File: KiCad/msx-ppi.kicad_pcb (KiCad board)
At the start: 2 copper layers, 85.1 x 63.9 mm, 17 parts, among them J1 Conn_02x13_Odd_Even, P1 CONN_02X25, Q1 BC547, SW1 DIPx8, U1 74HCT138, U2 74HCT32, U3 82C55A

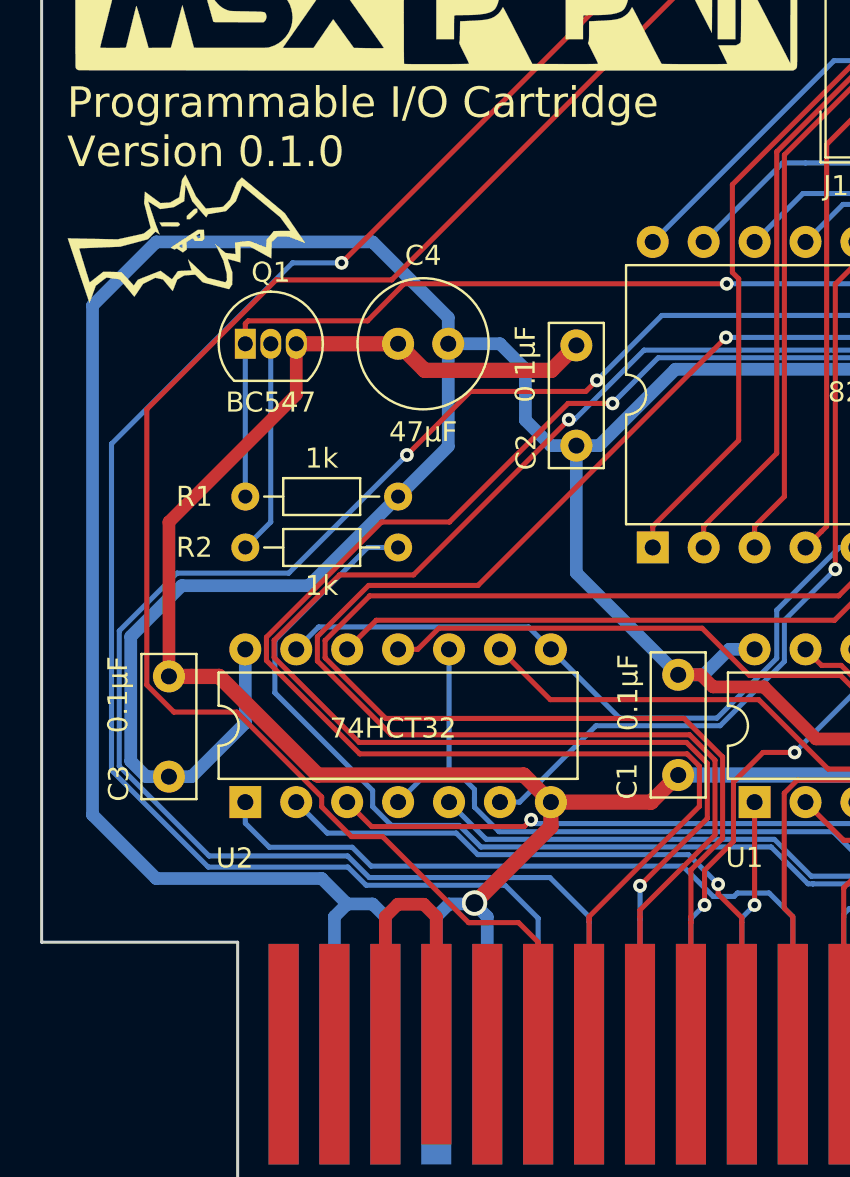
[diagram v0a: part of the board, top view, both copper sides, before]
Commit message: Changed Q1 footprint
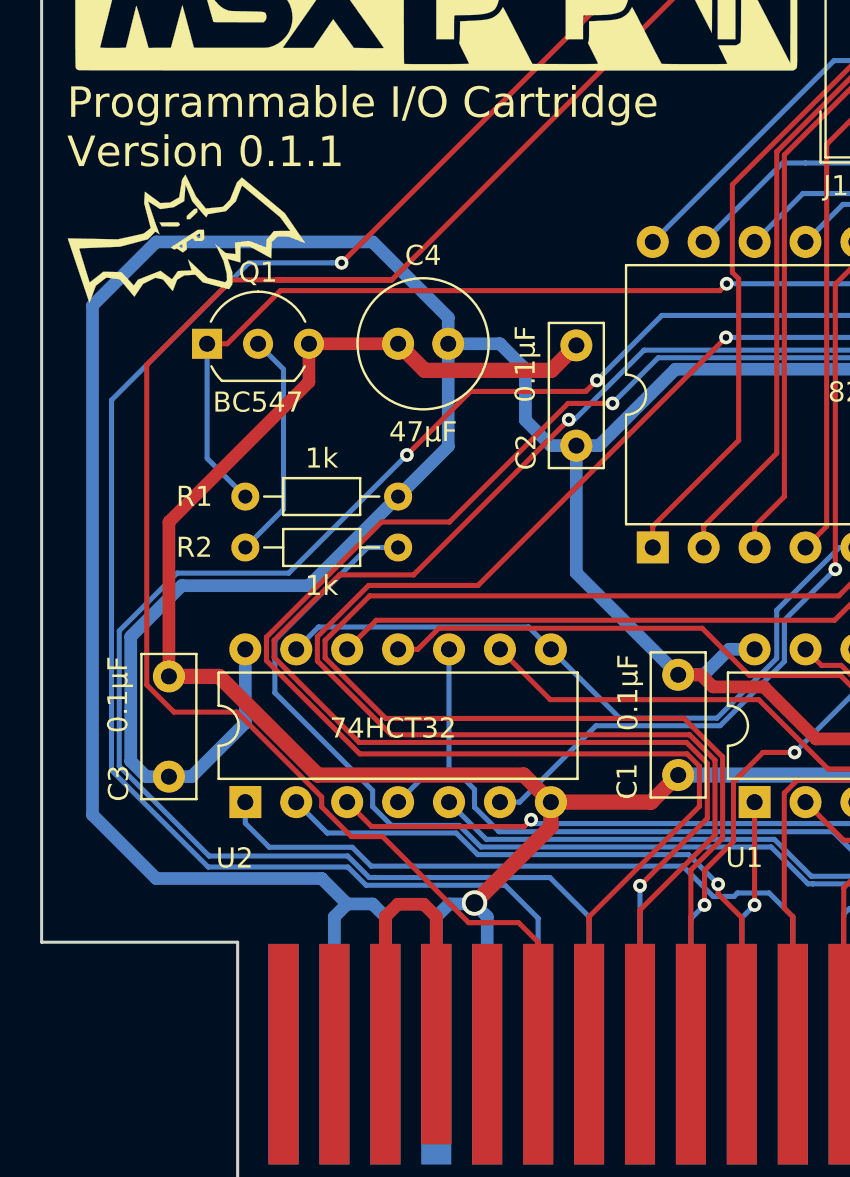
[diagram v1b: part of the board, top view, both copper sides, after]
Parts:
- Q1: footprint Package_TO_SOT_THT:TO-92_Inline -> Package_TO_SOT_THT:TO-92_Inline_Wide
- moved Q1 1.91 mm to (116.2, 87.0)
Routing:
- net D6: track 117.1 -> 124.2 mm
- net Net-(Q1-Pad1): track 43.3 -> 45.4 mm
- net D7: track 125.6 -> 126.9 mm
- net Net-(Q1-Pad2): track 10.7 -> 11.5 mm
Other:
- board text added: "Programmable I/O Cartridge Version 0.1.1"
- board text removed: "Programmable I/O Cartridge Version 0.1.0"

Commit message: Changed R2 value to 10k (was 1k)
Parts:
- R1: value 1k -> 10k
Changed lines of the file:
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@@
       (effects (font (size 1 1) (thickness 0.15)))
     )
-    (fp_text value 1k (at 3.81 1.905 180) (layer F.SilkS)
+    (fp_text value 10k (at 3.81 1.905 180) (layer F.SilkS)
       (effects (font (size 1 1) (thickness 0.15)))
     )
